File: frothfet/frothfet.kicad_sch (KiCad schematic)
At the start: 8 parts

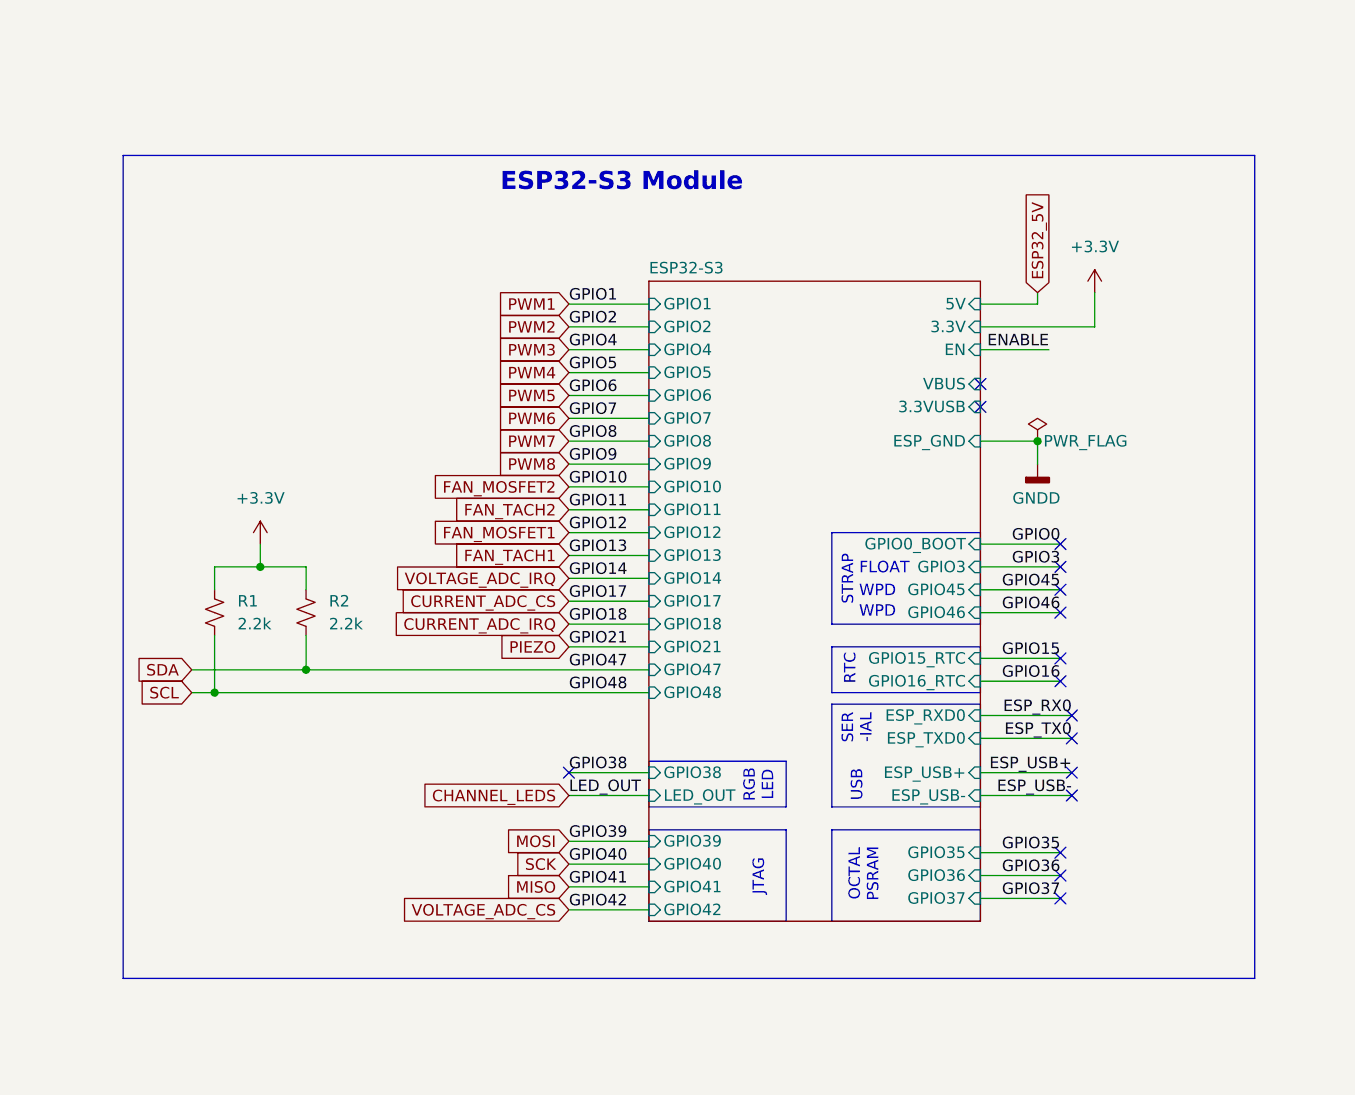
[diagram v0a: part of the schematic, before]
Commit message: updated calculations, updated esp32-s3 schematic, updated layout.
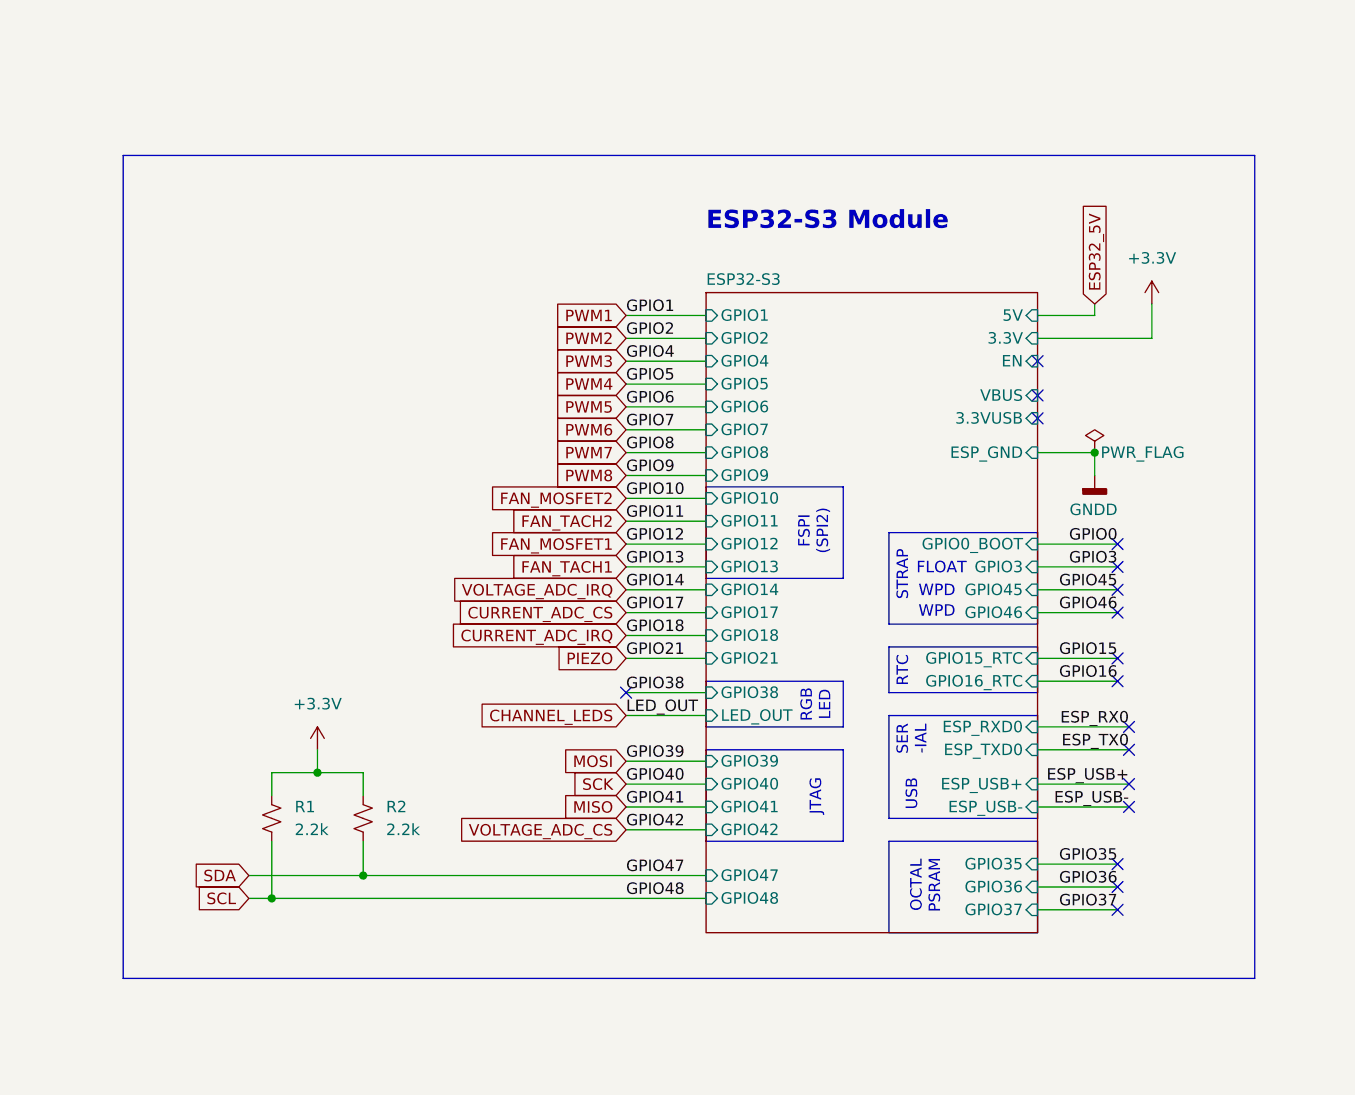
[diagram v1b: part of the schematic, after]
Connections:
- no-connect marks 17 -> 18
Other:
- note added: "FSPI (SPI2)"
- moved on the sheet: R1, R2

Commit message: worked on 3d models for all parts.
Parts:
- H1, H2, H3, H4: value MountingHole -> SMTSO30100CTJ; footprint MountingHole:MountingHole_3.2mm_M3_DIN965_Pad -> yarrboard:Standoff-3mm; now in the parts list
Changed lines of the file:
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@@
 		(unit 1)
 		(exclude_from_sim no)
-		(in_bom no)
+		(in_bom yes)
 		(on_board yes)
 		(dnp no)
@@
 			)
 		)
-		(property "Value" "MountingHole"
+		(property "Value" "SMTSO30100CTJ"
 			(at 21.59 162.56 90)
 			(effects
@@
 			)
 		)
-		(property "Footprint" "MountingHole:MountingHole_3.2mm_M3_DIN965_Pad"
+		(property "Footprint" "yarrboard:Standoff-3mm"
 			(at 22.86 166.37 0)
 			(effects
@@
 		(unit 1)
 		(exclude_from_sim no)
-		(in_bom no)
+		(in_bom yes)
 		(on_board yes)
 		(dnp no)
@@
 			)
 		)
-		(property "Value" "MountingHole"
+		(property "Value" "SMTSO30100CTJ"
 			(at 21.59 182.88 90)
 			(effects
@@
 			)
 		)
-		(property "Footprint" "MountingHole:MountingHole_3.2mm_M3_DIN965_Pad"
+		(property "Footprint" "yarrboard:Standoff-3mm"
 			(at 22.86 186.69 0)
 			(effects
@@
 		(unit 1)
 		(exclude_from_sim no)
-		(in_bom no)
+		(in_bom yes)
 		(on_board yes)
 		(dnp no)
@@
 			)
 		)
-		(property "Value" "MountingHole"
+		(property "Value" "SMTSO30100CTJ"
 			(at 21.59 151.13 90)
 			(effects
@@
 			)
 		)
-		(property "Footprint" "MountingHole:MountingHole_3.2mm_M3_DIN965_Pad"
+		(property "Footprint" "yarrboard:Standoff-3mm"
 			(at 22.86 154.94 0)
 			(effects
@@
 		(unit 1)
 		(exclude_from_sim no)
-		(in_bom no)
+		(in_bom yes)
 		(on_board yes)
 		(dnp no)
@@
 			)
 		)
-		(property "Value" "MountingHole"
+		(property "Value" "SMTSO30100CTJ"
 			(at 21.59 172.72 90)
 			(effects
@@
 			)
 		)
-		(property "Footprint" "MountingHole:MountingHole_3.2mm_M3_DIN965_Pad"
+		(property "Footprint" "yarrboard:Standoff-3mm"
 			(at 22.86 176.53 0)
 			(effects

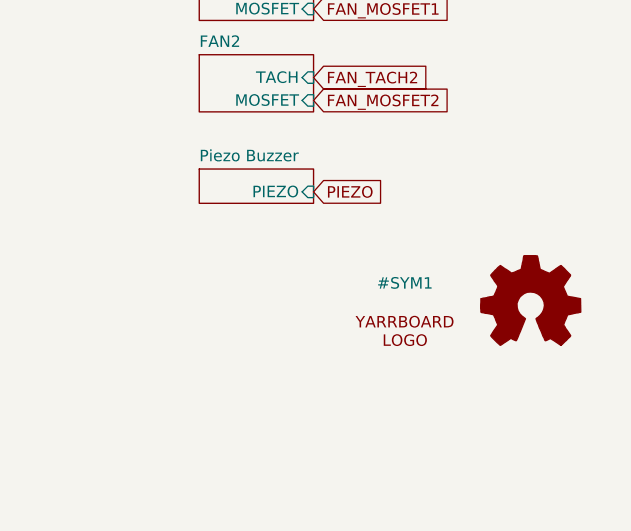
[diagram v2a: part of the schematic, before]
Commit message: worked on the bom and footprint placement
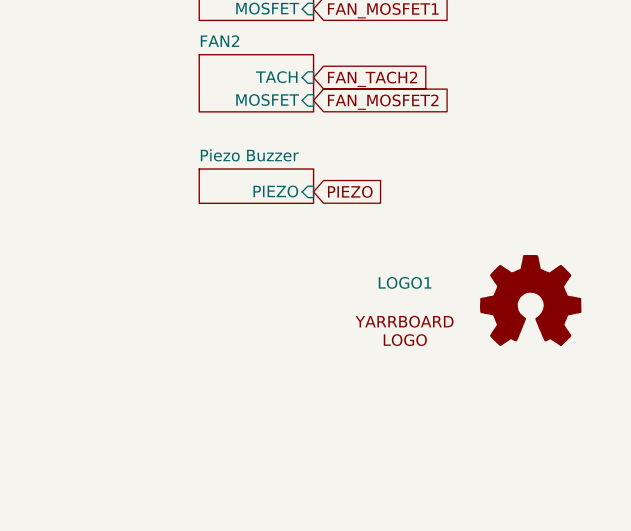
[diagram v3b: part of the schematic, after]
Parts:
- added LOGO1: ~, yarrboard:Logo Small, symbol yarrboard:Yarrboard
- R1, R2: LCSC C114561 -> (none)
- renumbered LOGO1 to LOGO2
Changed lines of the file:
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@@
 		(dnp no)
 		(fields_autoplaced yes)
-		(property "Reference" "#PWR0127"
+		(property "Reference" "#PWR04"
 			(at 139.7 59.69 0)
 			(effects
@@
 			(project "frothfet"
 				(path "/c83c6236-96e9-46ad-9d7a-9e2efa4a7966"
-					(reference "#PWR0127")
+					(reference "#PWR04")
 					(unit 1)
 				)
@@
 			)
 		)
-		(property "LCSC" "C114561"
+		(property "LCSC" ""
 			(at 41.91 113.03 0)
 			(effects
@@
 		(on_board yes)
 		(dnp no)
-		(property "Reference" "#PWR05"
+		(property "Reference" "#PWR03"
 			(at 133.35 81.28 0)
 			(effects
@@
 			(project "frothfet"
 				(path "/c83c6236-96e9-46ad-9d7a-9e2efa4a7966"
-					(reference "#PWR05")
+					(reference "#PWR03")
 					(unit 1)
 				)
@@
 		(dnp no)
 		(fields_autoplaced yes)
-		(property "Reference" "#SYM1"
+		(property "Reference" "LOGO1"
 			(at 261.62 171.45 0)
 			(effects
@@
 			(project ""
 				(path "/c83c6236-96e9-46ad-9d7a-9e2efa4a7966"
-					(reference "#SYM1")
+					(reference "LOGO1")
 					(unit 1)
 				)
@@
 			)
 		)
-		(property "LCSC" "C114561"
+		(property "LCSC" ""
 			(at 52.07 113.03 0)
 			(effects
@@
 		(dnp no)
 		(fields_autoplaced yes)
-		(property "Reference" "LOGO1"
+		(property "Reference" "LOGO2"
 			(at 275.59 167.005 0)
 			(effects
@@
 			(project ""
 				(path "/c83c6236-96e9-46ad-9d7a-9e2efa4a7966"
-					(reference "LOGO1")
-					(unit 1)
-				)
+					(reference "LOGO2")
+					(unit 1)
+				)

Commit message: lots of work on the analog system
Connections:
- net GNDD: no longer H3.1, H4.1
- new net GNDPWR: H3.1, H4.1
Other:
- moved on the sheet: H2, H4
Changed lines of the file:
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@@
 	)
 	(junction
-		(at 31.75 186.69)
+		(at 31.75 161.29)
 		(diameter 0)
 		(color 0 0 0 0)
 	)
 	(junction
-		(at 31.75 166.37)
+		(at 46.99 107.95)
 		(diameter 0)
 		(color 0 0 0 0)
 	)
 	(junction
-		(at 31.75 176.53)
+		(at 133.35 72.39)
 		(diameter 0)
 		(color 0 0 0 0)
 	)
 	(junction
-		(at 46.99 107.95)
+		(at 52.07 119.38)
 		(diameter 0)
 		(color 0 0 0 0)
 	)
 	(junction
-		(at 133.35 72.39)
-		(diameter 0)
-		(color 0 0 0 0)
-	)
-	(junction
-		(at 52.07 119.38)
+		(at 31.75 182.88)
 		(diameter 0)
 		(color 0 0 0 0)
@@
 	(wire
 		(pts
-			(xy 31.75 154.94) (xy 31.75 166.37)
+			(xy 31.75 154.94) (xy 31.75 161.29)
 		)
 		(stroke
@@
 	(wire
 		(pts
-			(xy 31.75 176.53) (xy 31.75 186.69)
-		)
-		(stroke
-			(width 0)
-			(type default)
-		)
-	)
-	(wire
-		(pts
 			(xy 243.84 81.28) (xy 246.38 81.28)
 		)
@@
 	(wire
 		(pts
-			(xy 25.4 176.53) (xy 31.75 176.53)
-		)
-		(stroke
-			(width 0)
-			(type default)
-		)
-	)
-	(wire
-		(pts
 			(xy 205.74 85.09) (xy 208.28 85.09)
 		)
@@
 	(wire
 		(pts
+			(xy 31.75 182.88) (xy 31.75 185.42)
+		)
+		(stroke
+			(width 0)
+			(type default)
+		)
+	)
+	(wire
+		(pts
 			(xy 90.17 59.69) (xy 81.28 59.69)
 		)
@@
 	(wire
 		(pts
-			(xy 31.75 166.37) (xy 31.75 176.53)
+			(xy 31.75 176.53) (xy 31.75 182.88)
 		)
 		(stroke
@@
 	(wire
 		(pts
-			(xy 261.62 68.58) (xy 259.08 68.58)
+			(xy 31.75 161.29) (xy 31.75 163.83)
 		)
 		(stroke
@@
 	(wire
 		(pts
-			(xy 208.28 49.53) (xy 208.28 53.34)
+			(xy 261.62 68.58) (xy 259.08 68.58)
 		)
 		(stroke
@@
 	(wire
 		(pts
-			(xy 127 123.19) (xy 135.89 123.19)
+			(xy 208.28 49.53) (xy 208.28 53.34)
 		)
 		(stroke
@@
 	(wire
 		(pts
-			(xy 127 59.69) (xy 139.7 59.69)
+			(xy 127 123.19) (xy 135.89 123.19)
 		)
 		(stroke
@@
 	(wire
 		(pts
-			(xy 261.62 71.12) (xy 259.08 71.12)
+			(xy 127 59.69) (xy 139.7 59.69)
 		)
 		(stroke
@@
 	(wire
 		(pts
-			(xy 243.84 71.12) (xy 246.38 71.12)
+			(xy 261.62 71.12) (xy 259.08 71.12)
 		)
 		(stroke
@@
 	(wire
 		(pts
-			(xy 25.4 186.69) (xy 31.75 186.69)
+			(xy 243.84 71.12) (xy 246.38 71.12)
 		)
 		(stroke
@@
 	(wire
 		(pts
-			(xy 31.75 186.69) (xy 31.75 191.77)
-		)
-		(stroke
-			(width 0)
-			(type default)
-		)
-	)
-	(wire
-		(pts
 			(xy 170.18 102.87) (xy 180.34 102.87)
 		)
@@
 	(wire
 		(pts
-			(xy 25.4 166.37) (xy 31.75 166.37)
+			(xy 25.4 161.29) (xy 31.75 161.29)
 		)
 		(stroke
@@
 	(wire
 		(pts
+			(xy 25.4 182.88) (xy 31.75 182.88)
+		)
+		(stroke
+			(width 0)
+			(type default)
+		)
+	)
+	(wire
+		(pts
 			(xy 205.74 120.65) (xy 208.28 120.65)
 		)
@@
 	(wire
 		(pts
+			(xy 25.4 176.53) (xy 31.75 176.53)
+		)
+		(stroke
+			(width 0)
+			(type default)
+		)
+	)
+	(wire
+		(pts
 			(xy 243.84 86.36) (xy 246.38 86.36)
 		)
@@
 	)
 	(symbol
+		(lib_id "power:GNDPWR")
+		(at 31.75 185.42 0)
+		(unit 1)
+		(exclude_from_sim no)
+		(in_bom yes)
+		(on_board yes)
+		(dnp no)
+		(fields_autoplaced yes)
+		(property "Reference" "#PWR0121"
+			(at 31.75 190.5 0)
+			(effects
+				(font
+					(size 1.27 1.27)
+				)
+				(hide yes)
+			)
+		)
+		(property "Value" "GNDPWR"
+			(at 31.623 189.23 0)
+			(effects
+				(font
+					(size 1.27 1.27)
+				)
+			)
+		)
+		(property "Footprint" ""
+			(at 31.75 186.69 0)
+			(effects
+				(font
+					(size 1.27 1.27)
+				)
+				(hide yes)
+			)
+		)
+		(property "Datasheet" ""
+			(at 31.75 186.69 0)
+			(effects
+				(font
+					(size 1.27 1.27)
+				)
+				(hide yes)
+			)
+		)
+		(property "Description" "Power symbol creates a global label with name \"GNDPWR\" , global ground"
+			(at 31.75 185.42 0)
+			(effects
+				(font
+					(size 1.27 1.27)
+				)
+				(hide yes)
+			)
+		)
+		(pin "1"
+		)
+		(instances
+			(project "frothfet"
+				(path "/c83c6236-96e9-46ad-9d7a-9e2efa4a7966"
+					(reference "#PWR0121")
+					(unit 1)
+				)
+			)
+		)
+	)
+	(symbol
 		(lib_id "Device:R_Small_US")
 		(at 41.91 113.03 180)
@@
 	(symbol
 		(lib_id "Mechanical:MountingHole_Pad")
-		(at 22.86 166.37 90)
+		(at 22.86 161.29 90)
 		(unit 1)
 		(exclude_from_sim no)
@@
 		(on_board yes)
 		(dnp no)
-		(fields_autoplaced yes)
 		(property "Reference" "H2"
-			(at 21.59 160.02 90)
+			(at 21.59 158.496 90)
 			(effects
 				(font
@@
 		)
 		(property "Value" "SMTSO30100CTJ"
-			(at 21.59 162.56 90)
+			(at 21.59 157.48 90)
 			(effects
 				(font
 					(size 1.27 1.27)
 				)
+				(hide yes)
 			)
 		)
 		(property "Footprint" "yarrboard:Standoff-3mm"
-			(at 22.86 166.37 0)
+			(at 22.86 161.29 0)
 			(effects
 				(font
@@
 		)
 		(property "Datasheet" "~"
-			(at 22.86 166.37 0)
+			(at 22.86 161.29 0)
 			(effects
 				(font
@@
 		)
 		(property "Description" ""
-			(at 22.86 166.37 0)
+			(at 22.86 161.29 0)
 			(effects
 				(font
@@
 		)
 		(property "ALT" ""
-			(at 22.86 166.37 0)
+			(at 22.86 161.29 0)
 			(effects
 				(font
@@
 	(symbol
 		(lib_id "Mechanical:MountingHole_Pad")
-		(at 22.86 186.69 90)
+		(at 22.86 182.88 90)
 		(unit 1)
 		(exclude_from_sim no)
@@
 		(on_board yes)
 		(dnp no)
-		(fields_autoplaced yes)
 		(property "Reference" "H4"
-			(at 21.59 180.34 90)
+			(at 21.59 179.832 90)
 			(effects
 				(font
@@
 		)
 		(property "Value" "SMTSO30100CTJ"
-			(at 21.59 182.88 90)
+			(at 21.59 179.07 90)
 			(effects
 				(font
 					(size 1.27 1.27)
 				)
+				(hide yes)
 			)
 		)
 		(property "Footprint" "yarrboard:Standoff-3mm"
-			(at 22.86 186.69 0)
+			(at 22.86 182.88 0)
 			(effects
 				(font
@@
 		)
 		(property "Datasheet" "~"
-			(at 22.86 186.69 0)
+			(at 22.86 182.88 0)
 			(effects
 				(font
@@
 		)
 		(property "Description" ""
-			(at 22.86 186.69 0)
+			(at 22.86 182.88 0)
 			(effects
 				(font
@@
 		)
 		(property "ALT" ""
-			(at 22.86 186.69 0)
+			(at 22.86 182.88 0)
 			(effects
 				(font
@@
 		(on_board yes)
 		(dnp no)
-		(fields_autoplaced yes)
 		(property "Reference" "H1"
-			(at 21.59 148.59 90)
+			(at 21.59 151.892 90)
 			(effects
 				(font
@@
 					(size 1.27 1.27)
 				)
+				(hide yes)
 			)
 		)
@@
 	(symbol
 		(lib_id "power:GNDD")
-		(at 31.75 191.77 0)
+		(at 31.75 163.83 0)
 		(unit 1)
 		(exclude_from_sim no)
@@
 		(dnp no)
 		(property "Reference" "#PWR01"
-			(at 31.75 198.12 0)
+			(at 31.75 170.18 0)
 			(effects
 				(font
@@
 		)
 		(property "Value" "GNDD"
-			(at 34.29 195.58 0)
+			(at 34.29 167.64 0)
 			(effects
 				(font
@@
 		)
 		(property "Footprint" ""
-			(at 31.75 191.77 0)
+			(at 31.75 163.83 0)
 			(effects
 				(font
@@
 		)
 		(property "Datasheet" ""
-			(at 31.75 191.77 0)
+			(at 31.75 163.83 0)
 			(effects
 				(font
@@
 		)
 		(property "Description" "Power symbol creates a global label with name \"GNDD\" , digital ground"
-			(at 31.75 191.77 0)
+			(at 31.75 163.83 0)
 			(effects
 				(font
@@
 		(dnp no)
 		(property "Reference" "H3"
-			(at 21.59 170.18 90)
+			(at 21.59 173.736 90)
 			(effects
 				(font
@@
 					(size 1.27 1.27)
 				)
+				(hide yes)
 			)
 		)

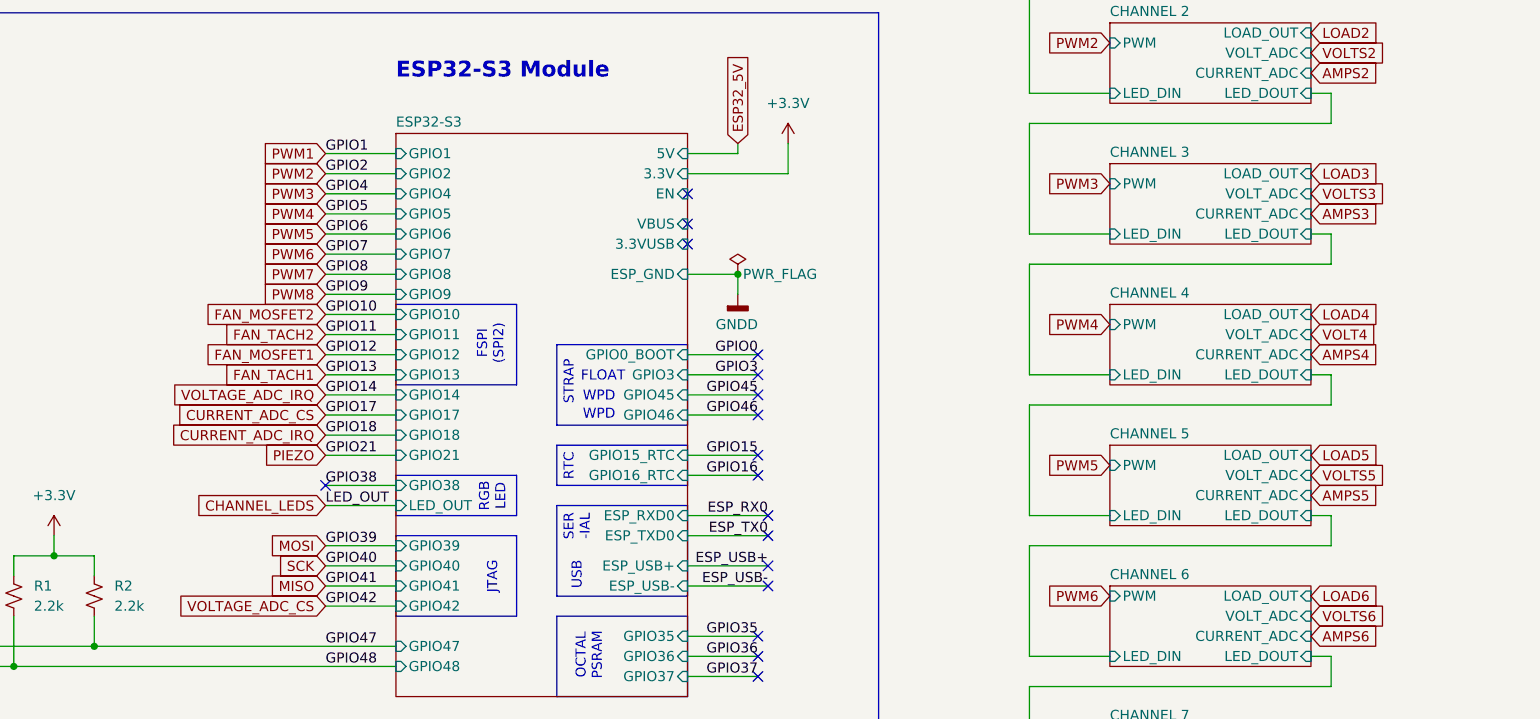
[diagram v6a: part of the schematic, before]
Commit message: finished re-routing the board.
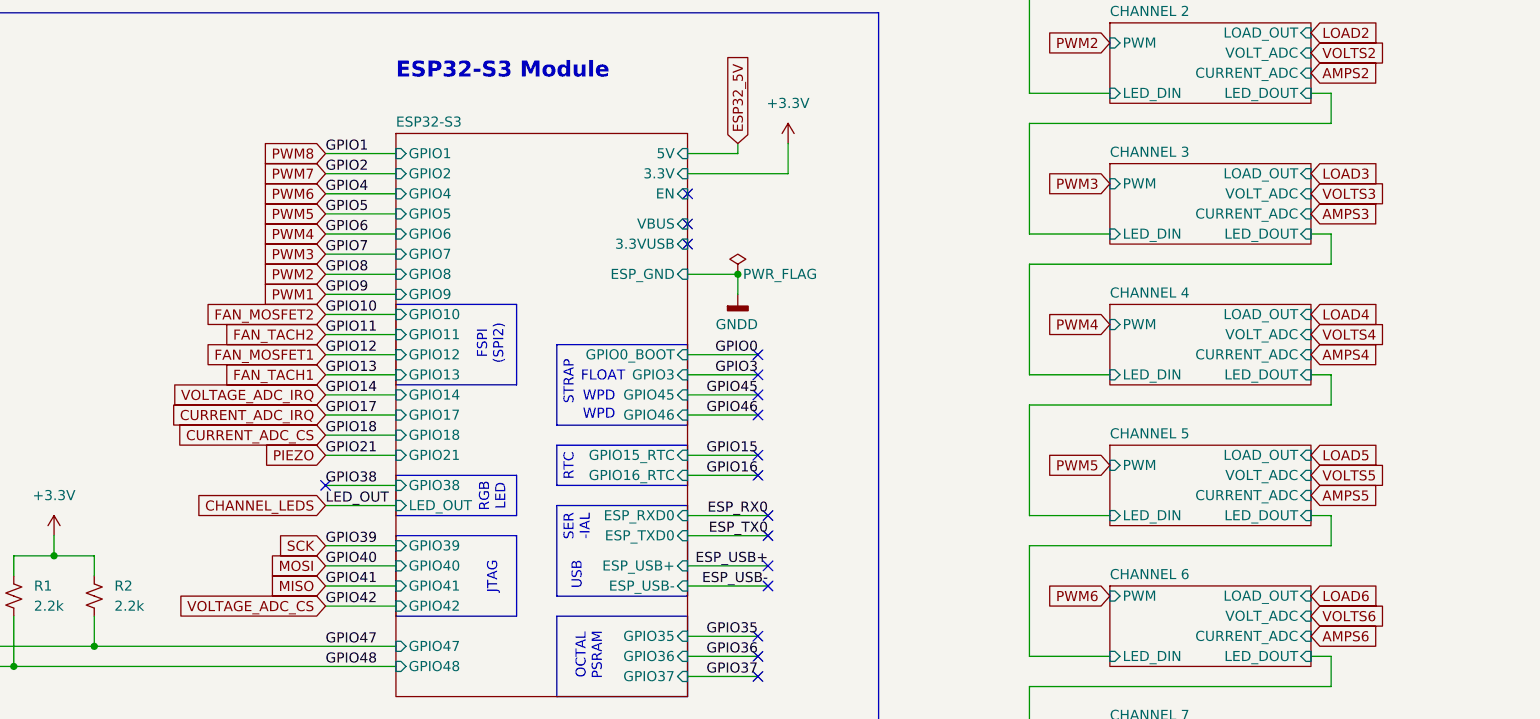
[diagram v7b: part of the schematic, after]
